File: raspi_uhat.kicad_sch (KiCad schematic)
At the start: 22 parts, among them J1 FH35C-45S-0.3SHW(50), J2 FH35C-45S-0.3SHW(50), J3 GPIO, J4 Conn_01x03_Socket, J5 Conn_01x03_Socket, J6 Conn_01x03_Socket, J7 Conn_01x03_Socket, J8 Conn_01x03_Socket, U1 FODM217D, U2 FODM217D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

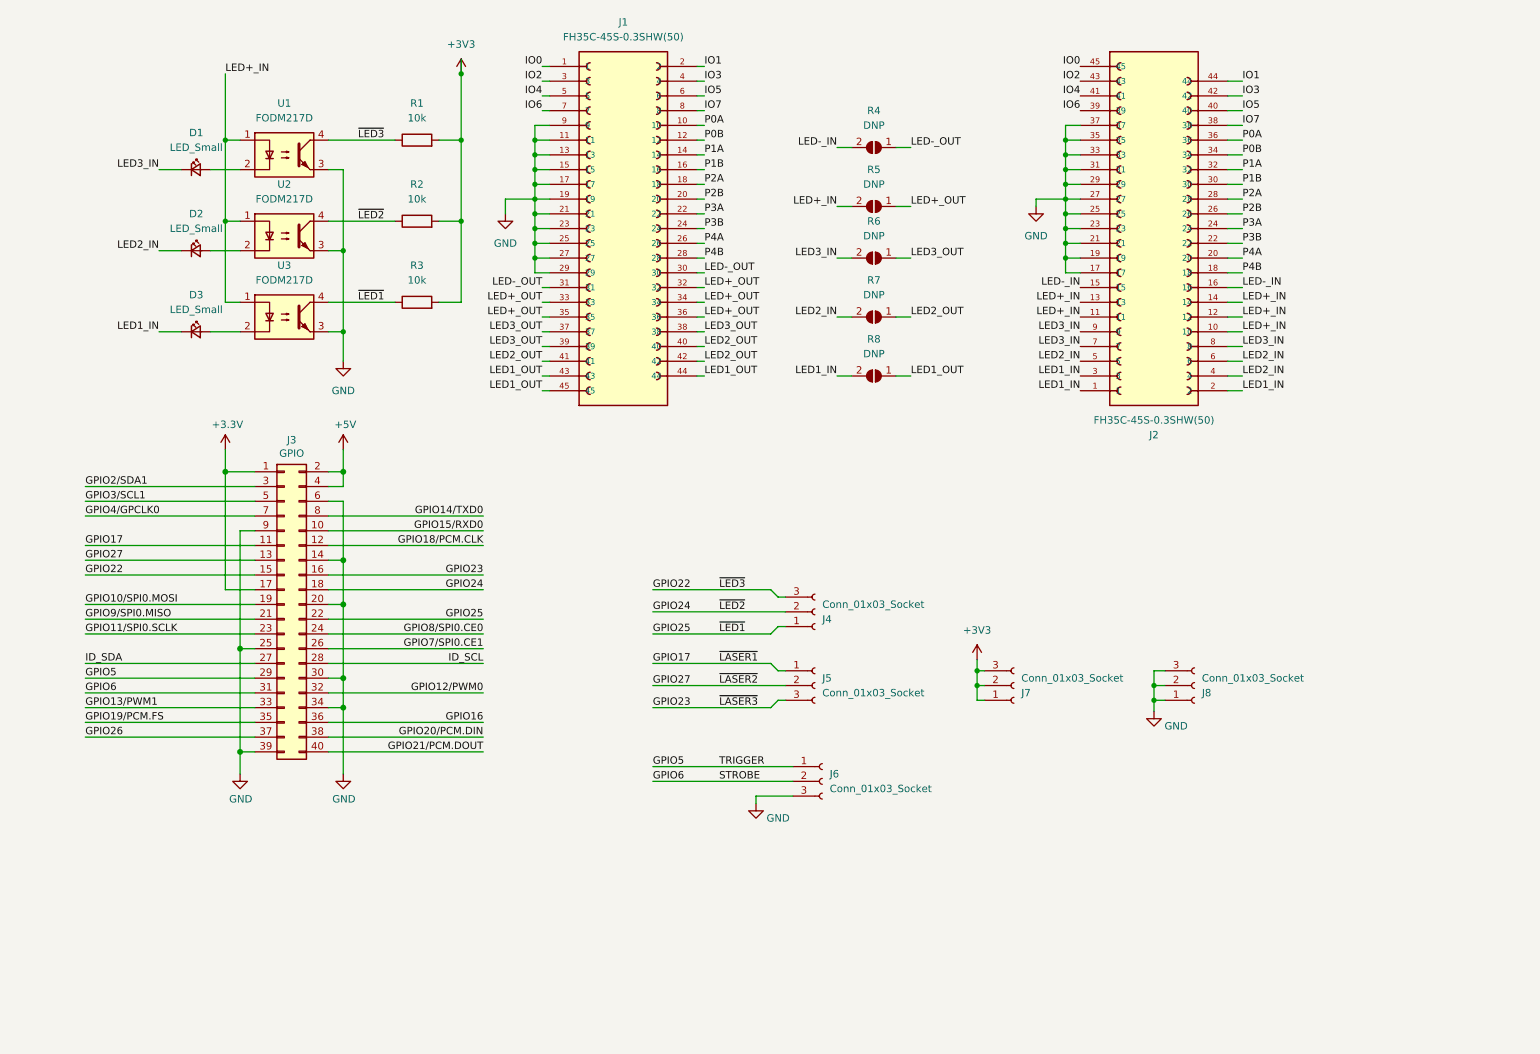
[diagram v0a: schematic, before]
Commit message: Redesigned as Raspberry Pi (Zero) hat
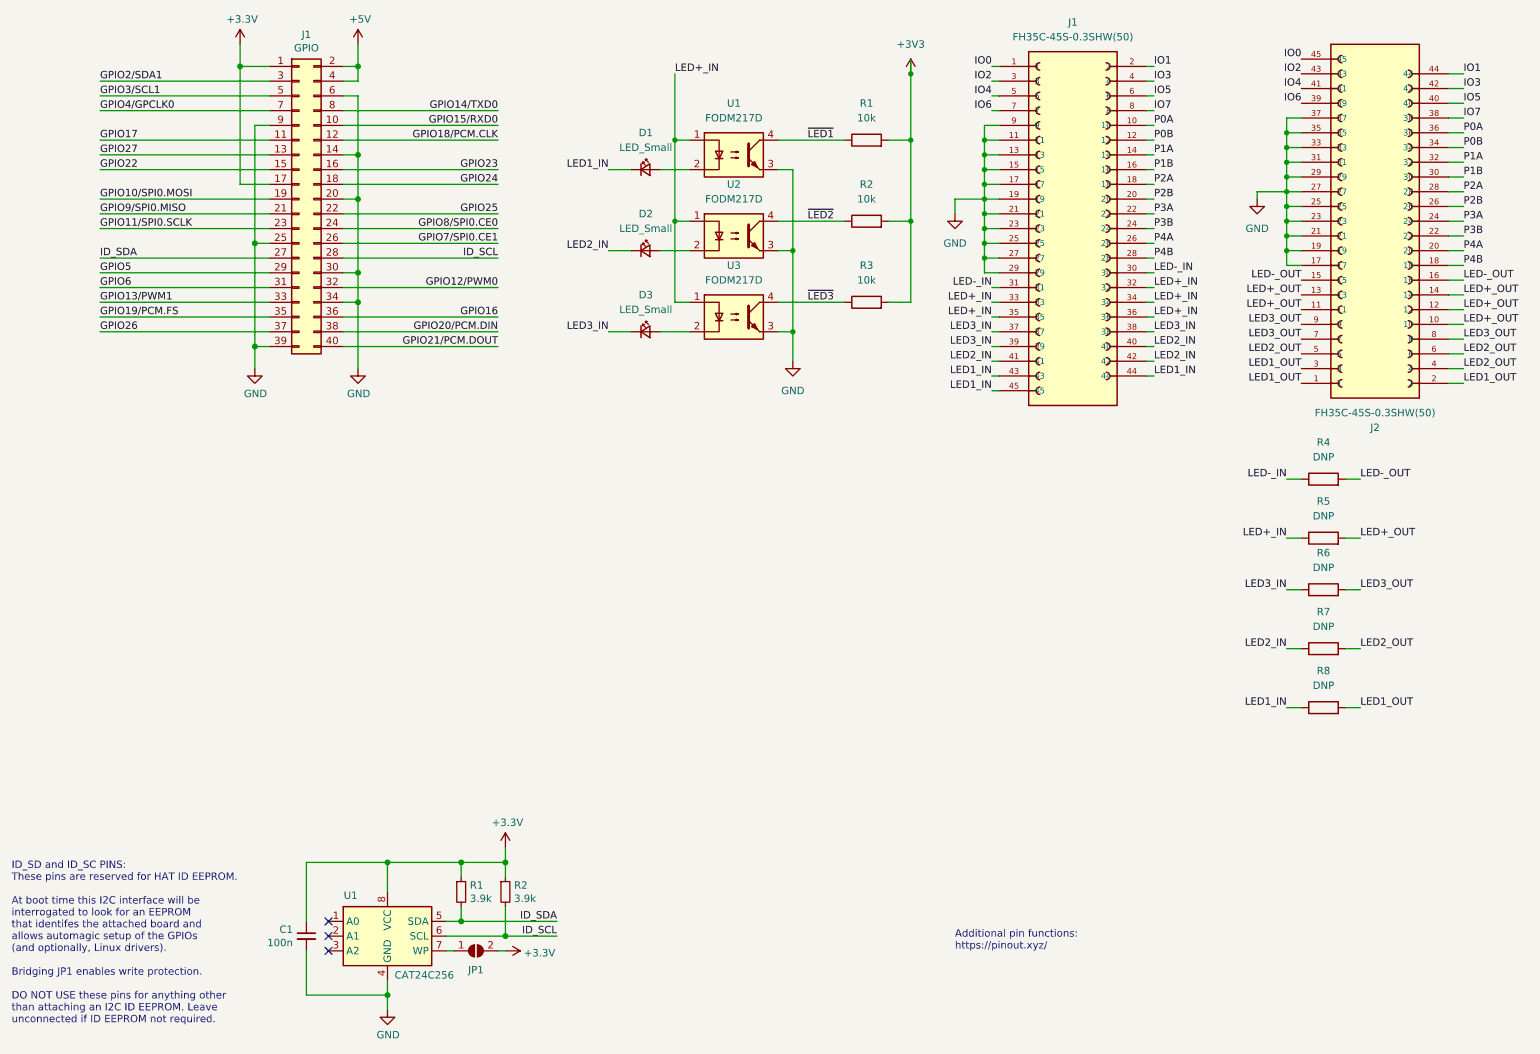
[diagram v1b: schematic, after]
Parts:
- removed J3: GPIO, Connector_PinSocket_2.54mm:PinSocket_2x20_P2.54mm_Vertical, symbol Connector_Generic:Conn_02x20_Odd_Even
- removed J4, J5, J6, J7, J8: Conn_01x03_Socket, Connector_PinSocket_2.54mm:PinSocket_1x03_P2.54mm_Vertical_SMD_Pin1Right, symbol Connector:Conn_01x03_Socket
- removed R4, R5, R6, R7, R8: DNP, Resistor_SMD:R_0402_1005Metric, symbol Jumper:SolderJumper_2_Open
- added C1: 100n, symbol Device:C_Small
- added J1: GPIO, Connector_PinSocket_2.54mm:PinSocket_2x20_P2.54mm_Vertical, symbol Connector_Generic:Conn_02x20_Odd_Even
- added JP1: ID_WP, symbol Jumper:SolderJumper_2_Open
- added R1, R2: 3.9k, symbol Device:R_Small
- added R4, R5, R6, R7, R8: DNP, Resistor_SMD:R_0603_1608Metric, symbol Device:R
- added U1: CAT24C256, symbol Memory_EEPROM:CAT24C256
- D1, D2, D3: footprint LED_SMD:LED_1206_3216Metric_Pad1.42x1.75mm_HandSolder -> LED_SMD:LED_0603_1608Metric_Pad1.05x0.95mm_HandSolder
- R1, R2, R3: footprint Resistor_SMD:R_1206_3216Metric_Pad1.30x1.75mm_HandSolder -> Resistor_SMD:R_0603_1608Metric
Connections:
- net +3V3: now also C1.1, J1.1 (Pin_1), J1.17 (Pin_17), JP1.2 (B), R1.1, R2.1, U1.8 (VCC)
- net +5V: now also J1.2 (Pin_2), J1.4 (Pin_4)
- net GND: now also C1.2, J1.14 (Pin_14), J1.20 (Pin_20), J1.25 (Pin_25), J1.30 (Pin_30), J1.34 (Pin_34), J1.39 (Pin_39), J1.6 (Pin_6), J1.9 (Pin_9), U1.4 (GND)
- net GPIO10/SPI0.MOSI: now also J1.19 (Pin_19)
- net GPIO11/SPI0.SCLK: now also J1.23 (Pin_23)
- net GPIO12/PWM0: now also J1.32 (Pin_32)
- net GPIO13/PWM1: now also J1.33 (Pin_33)
- net GPIO14/TXD0: now also J1.8 (Pin_8)
- net GPIO15/RXD0: now also J1.10 (Pin_10)
- net GPIO16: now also J1.36 (Pin_36)
- net GPIO17: now also J1.11 (Pin_11)
- net GPIO18/PCM.CLK: now also J1.12 (Pin_12)
- net GPIO19/PCM.FS: now also J1.35 (Pin_35)
- net GPIO20/PCM.DIN: now also J1.38 (Pin_38)
- net GPIO21/PCM.DOUT: now also J1.40 (Pin_40)
- net GPIO22: now also J1.15 (Pin_15); no longer R1.1, U1.4
- net GPIO23: now also J1.16 (Pin_16)
- net GPIO24: now also J1.18 (Pin_18); no longer R2.1, U2.4
- net GPIO25: now also J1.22 (Pin_22); no longer R3.1, U3.4
- net GPIO26: now also J1.37 (Pin_37)
- net GPIO27: now also J1.13 (Pin_13)
- net GPIO2/SDA1: now also J1.3 (Pin_3)
- net GPIO3/SCL1: now also J1.5 (Pin_5)
- net GPIO4/GPCLK0: now also J1.7 (Pin_7)
- net GPIO5: now also J1.29 (Pin_29)
- net GPIO6: now also J1.31 (Pin_31)
- net GPIO7/SPI0.CE1: now also J1.26 (Pin_26)
- net GPIO8/SPI0.CE0: now also J1.24 (Pin_24)
- net GPIO9/SPI0.MISO: now also J1.21 (Pin_21)
- net ID_SCL: now also J1.28 (Pin_28), R2.2, U1.6 (SCL)
- net ID_SDA: now also J1.27 (Pin_27), R1.2, U1.5 (SDA)
- net LED+_IN: now also J1.32, J1.33, J1.34, J1.35, J1.36, R5.1; no longer J2.10, J2.11, J2.12, J2.13, J2.14
- net LED+_OUT: now also J2.10, J2.11, J2.12, J2.13, J2.14, R5.2; no longer J1.32, J1.33, J1.34, J1.35, J1.36
- net LED-_IN: now also J1.30, J1.31, R4.1; no longer J2.15, J2.16
- net LED-_OUT: now also J2.15, J2.16, R4.2; no longer J1.30, J1.31
- net LED1_IN: now also D1.1 (K), J1.43, J1.44, J1.45, R8.1; no longer D3.1 (K), J2.1, J2.2, J2.3
- net LED1_OUT: now also J2.1, J2.2, J2.3, R8.2; no longer J1.43, J1.44, J1.45
- net LED2_IN: now also J1.40, J1.41, J1.42, R7.1; no longer J2.4, J2.5, J2.6
- net LED2_OUT: now also J2.4, J2.5, J2.6, R7.2; no longer J1.40, J1.41, J1.42
- net LED3_IN: now also D3.1 (K), J1.37, J1.38, J1.39, R6.1; no longer D1.1 (K), J2.7, J2.8, J2.9
- net LED3_OUT: now also J2.7, J2.8, J2.9, R6.2; no longer J1.37, J1.38, J1.39
- new net: JP1.1 (A), U1.7 (WP)
- new net ~{LED1}: R1.1, U1.4
- new net ~{LED2}: R2.1, U2.4
- new net ~{LED3}: R3.1, U3.4
- no-connect marks 0 -> 3
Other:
- note added: "Additional pin functions: https://pinout.xyz/"
- note added: "ID_SD and ID_SC PINS: These pins are reserved for HAT ID EEPROM. At boot time this I2C interface will be interrogated to look for an EEPROM that identifes the attached board and allows automagic setup of the GPIOs (and optionally, Linux drivers). Bridging JP1 enables write protection. DO NOT USE these pins for anything other than attaching an I2C ID EEPROM. Leave unconnected if ID EEPROM not requ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"
